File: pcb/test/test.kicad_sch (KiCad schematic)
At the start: 27 parts, among them IC1 ADG904BRUZ-REEL7, J1 CONSMA013.062-G, J3 Conn_01x04, U2 TL081

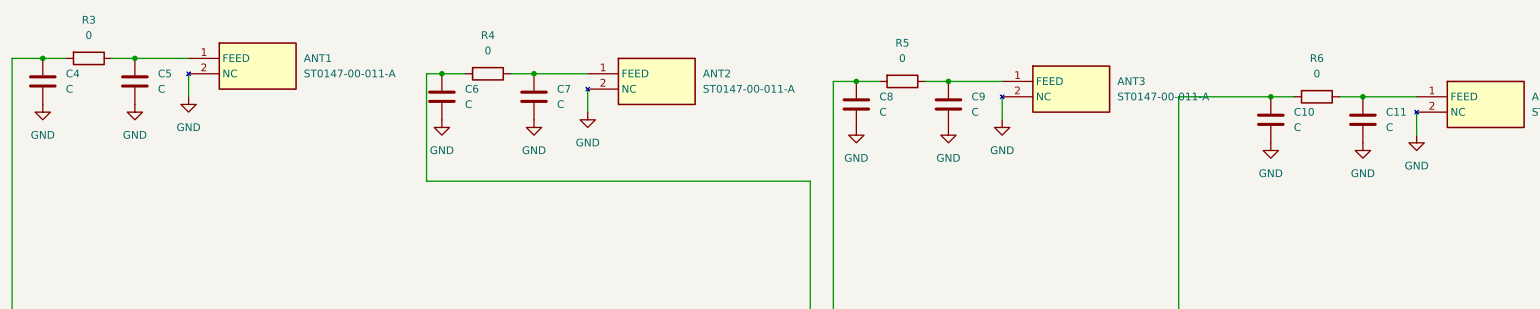
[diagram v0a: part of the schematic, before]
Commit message: routage guides d'onde
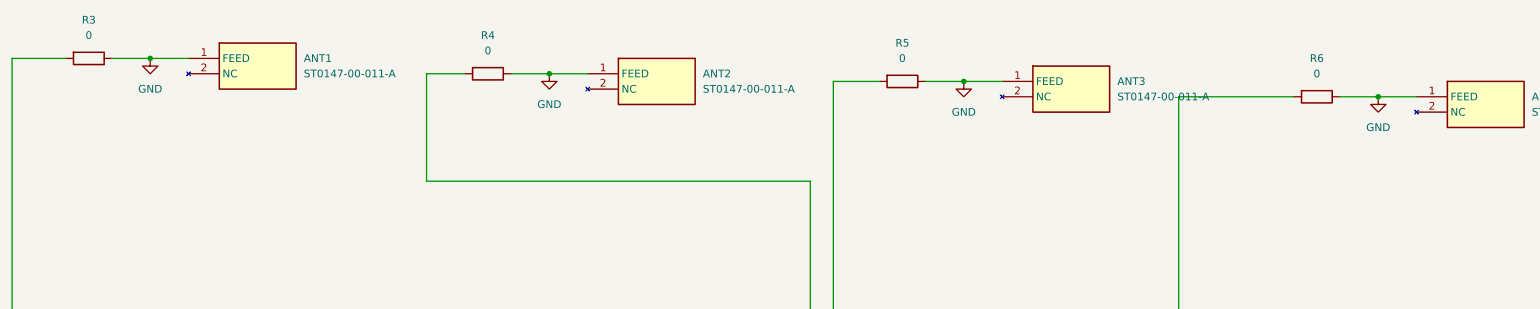
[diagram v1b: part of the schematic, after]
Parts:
- removed C10, C11, C4, C5, C6, C7, C8, C9: C, Capacitor_SMD:C_0201_0603Metric, symbol Device:C
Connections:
- net GND: now also ANT1.1 (FEED), ANT2.1 (FEED), ANT3.1 (FEED), ANT4.1 (FEED), R3.1, R4.1, R5.1, R6.1; no longer ANT1.2 (NC), ANT2.2 (NC), ANT3.2 (NC), ANT4.2 (NC)

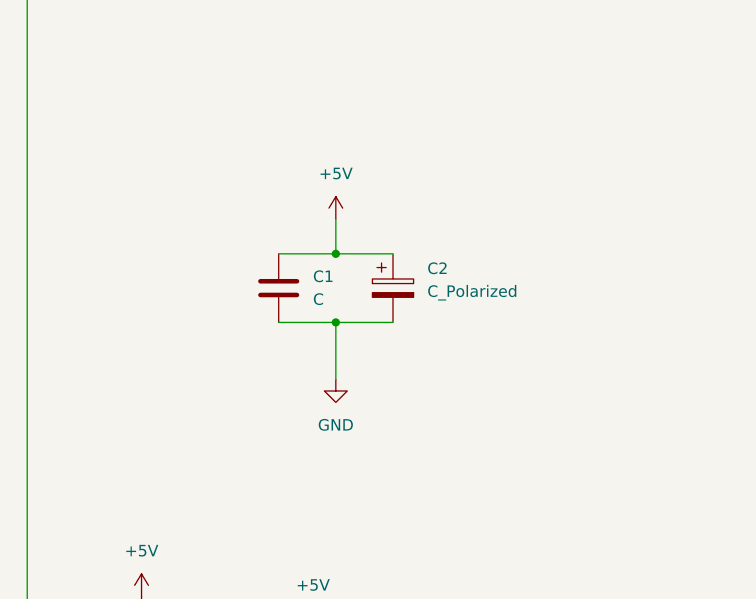
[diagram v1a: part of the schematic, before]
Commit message: composants pour 2V5 placés
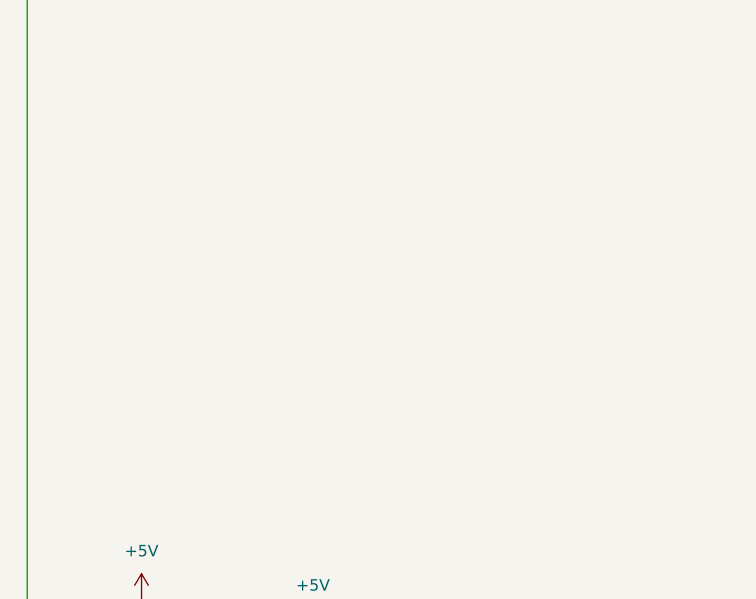
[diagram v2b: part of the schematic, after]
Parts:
- removed C1: C, Capacitor_SMD:CP_Elec_6.3x5.4, symbol Device:C
- removed C2: C_Polarized, Capacitor_SMD:CP_Elec_6.3x5.4, symbol Device:C_Polarized
- C3: footprint Capacitor_SMD:CP_Elec_6.3x5.4 -> Capacitor_THT:CP_Radial_D8.0mm_P5.00mm

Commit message: beaucoup vias
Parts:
- removed JP2: Jumper_2_Bridged, test_footprint_library:jumper20, symbol Jumper:Jumper_2_Bridged
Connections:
- net +2V5: now also JP1.1 (A); no longer IC1.2 (VDD)
- net +5V: now also J3.2 (Pin_2); no longer J3.1 (Pin_1)
- net GND: now also J3.1 (Pin_1); no longer J3.2 (Pin_2)
- net at IC1.20 (A0): now also J3.4 (Pin_4)
- net at J3.3 (Pin_3): now also IC1.19 (A1)
- net at JP1.2 (B): now also IC1.2 (VDD); no longer J3.4 (Pin_4)
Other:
- moved on the sheet: JP1
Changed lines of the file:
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@@
-	(wire
-		(pts
-			(xy 170.18 180.34) (xy 162.56 180.34)
-		)
-		(stroke
-			(width 0)
-			(type default)
-		)
-	)
 	(wire
 		(pts
@@
 	(wire
 		(pts
-			(xy 148.59 182.88) (xy 146.05 182.88)
-		)
-		(stroke
-			(width 0)
-			(type default)
-		)
-	)
-	(wire
-		(pts
 			(xy 172.72 31.75) (xy 179.07 31.75)
 		)
@@
 	(wire
 		(pts
-			(xy 162.56 180.34) (xy 162.56 189.23)
-		)
-		(stroke
-			(width 0)
-			(type default)
-		)
-	)
-	(wire
-		(pts
 			(xy 31.75 27.94) (xy 38.1 27.94)
 		)
@@
 	(wire
 		(pts
-			(xy 160.02 182.88) (xy 158.75 182.88)
-		)
-		(stroke
-			(width 0)
-			(type default)
-		)
-	)
-	(wire
-		(pts
 			(xy 140.97 143.51) (xy 148.59 143.51)
 		)
@@
 	(wire
 		(pts
-			(xy 146.05 182.88) (xy 146.05 123.19)
-		)
-		(stroke
-			(width 0)
-			(type default)
-		)
-	)
-	(wire
-		(pts
 			(xy 92.71 133.35) (xy 92.71 135.89)
 		)
@@
 	(wire
 		(pts
+			(xy 146.05 123.19) (xy 146.05 185.42)
+		)
+		(stroke
+			(width 0)
+			(type default)
+		)
+	)
+	(wire
+		(pts
+			(xy 165.1 189.23) (xy 165.1 187.96)
+		)
+		(stroke
+			(width 0)
+			(type default)
+		)
+	)
+	(wire
+		(pts
+			(xy 143.51 182.88) (xy 160.02 182.88)
+		)
+		(stroke
+			(width 0)
+			(type default)
+		)
+	)
+	(wire
+		(pts
 			(xy 99.06 138.43) (xy 99.06 161.29)
 		)
@@
 	(wire
 		(pts
-			(xy 71.12 128.27) (xy 81.28 128.27)
-		)
-		(stroke
-			(width 0)
-			(type default)
-		)
-	)
-	(wire
-		(pts
 			(xy 148.59 140.97) (xy 148.59 143.51)
 		)
@@
 	(wire
 		(pts
-			(xy 143.51 185.42) (xy 143.51 125.73)
-		)
-		(stroke
-			(width 0)
-			(type default)
-		)
-	)
-	(wire
-		(pts
 			(xy 151.13 161.29) (xy 151.13 31.75)
 		)
@@
 	(wire
 		(pts
-			(xy 157.48 185.42) (xy 154.94 185.42)
-		)
-		(stroke
-			(width 0)
-			(type default)
-		)
-	)
-	(wire
-		(pts
 			(xy 92.71 143.51) (xy 107.95 143.51)
 		)
@@
 	(wire
 		(pts
+			(xy 157.48 185.42) (xy 146.05 185.42)
+		)
+		(stroke
+			(width 0)
+			(type default)
+		)
+	)
+	(wire
+		(pts
 			(xy 148.59 135.89) (xy 148.59 140.97)
 		)
@@
 	(wire
 		(pts
-			(xy 165.1 189.23) (xy 173.99 189.23)
-		)
-		(stroke
-			(width 0)
-			(type default)
-		)
-	)
-	(wire
-		(pts
 			(xy 92.71 140.97) (xy 92.71 143.51)
 		)
@@
 	(wire
 		(pts
+			(xy 165.1 187.96) (xy 170.18 187.96)
+		)
+		(stroke
+			(width 0)
+			(type default)
+		)
+	)
+	(wire
+		(pts
 			(xy 92.71 116.84) (xy 92.71 123.19)
 		)
@@
 	(wire
 		(pts
+			(xy 143.51 182.88) (xy 143.51 125.73)
+		)
+		(stroke
+			(width 0)
+			(type default)
+		)
+	)
+	(wire
+		(pts
 			(xy 99.06 161.29) (xy 151.13 161.29)
 		)
@@
 	(wire
 		(pts
-			(xy 144.78 185.42) (xy 143.51 185.42)
-		)
-		(stroke
-			(width 0)
-			(type default)
-		)
-	)
-	(wire
-		(pts
 			(xy 83.82 48.26) (xy 83.82 30.48)
 		)
@@
 		(pts
 			(xy 208.28 138.43) (xy 208.28 34.29)
-		)
-		(stroke
-			(width 0)
-			(type default)
-		)
-	)
-	(wire
-		(pts
-			(xy 173.99 189.23) (xy 173.99 177.8)
 		)
 		(stroke
@@
 	)
 	(symbol
-		(lib_id "Jumper:Jumper_2_Bridged")
-		(at 153.67 182.88 0)
-		(unit 1)
-		(exclude_from_sim yes)
-		(in_bom yes)
-		(on_board yes)
-		(dnp no)
-		(fields_autoplaced yes)
-		(property "Reference" "JP2"
-			(at 153.67 177.8 0)
-			(effects
-				(font
-					(size 1.27 1.27)
-				)
-			)
-		)
-		(property "Value" "Jumper_2_Bridged"
-			(at 153.67 180.34 0)
-			(effects
-				(font
-					(size 1.27 1.27)
-				)
-				(hide yes)
-			)
-		)
-		(property "Footprint" "test_footprint_library:jumper20"
-			(at 153.67 182.88 0)
-			(effects
-				(font
-					(size 1.27 1.27)
-				)
-				(hide yes)
-			)
-		)
-		(property "Datasheet" "~"
-			(at 153.67 182.88 0)
-			(effects
-				(font
-					(size 1.27 1.27)
-				)
-				(hide yes)
-			)
-		)
-		(property "Description" "Jumper, 2-pole, closed/bridged"
-			(at 153.67 182.88 0)
-			(effects
-				(font
-					(size 1.27 1.27)
-				)
-				(hide yes)
-			)
-		)
-		(pin "2"
-		)
-		(pin "1"
-		)
-		(instances
-			(project "test"
-				(path "/bb1015a8-5dcf-444f-b1dc-3665f721c6b4"
-					(reference "JP2")
-					(unit 1)
-				)
-			)
-		)
-	)
-	(symbol
 		(lib_id "power:GND")
 		(at 241.3 34.29 0)
@@
 	(symbol
 		(lib_id "Jumper:Jumper_2_Bridged")
-		(at 149.86 185.42 0)
+		(at 76.2 128.27 0)
 		(unit 1)
 		(exclude_from_sim yes)
@@
 		(fields_autoplaced yes)
 		(property "Reference" "JP1"
-			(at 149.86 180.34 0)
+			(at 76.2 123.19 0)
 			(effects
 				(font
@@
 		)
 		(property "Value" "Jumper_2_Bridged"
-			(at 149.86 182.88 0)
+			(at 76.2 125.73 0)
 			(effects
 				(font
@@
 		)
 		(property "Footprint" "test_footprint_library:jumper20"
-			(at 149.86 185.42 0)
+			(at 76.2 128.27 0)
 			(effects
 				(font
@@
 		)
 		(property "Datasheet" "~"
-			(at 149.86 185.42 0)
+			(at 76.2 128.27 0)
 			(effects
 				(font
@@
 		)
 		(property "Description" "Jumper, 2-pole, closed/bridged"
-			(at 149.86 185.42 0)
+			(at 76.2 128.27 0)
 			(effects
 				(font
@@
 	(symbol
 		(lib_id "power:+5V")
-		(at 173.99 177.8 0)
+		(at 162.56 189.23 0)
 		(unit 1)
 		(exclude_from_sim no)
@@
 		(fields_autoplaced yes)
 		(property "Reference" "#PWR01"
-			(at 173.99 181.61 0)
+			(at 162.56 193.04 0)
 			(effects
 				(font
@@
 		)
 		(property "Value" "+5V"
-			(at 173.99 172.72 0)
+			(at 162.56 184.15 0)
 			(effects
 				(font
@@
 		)
 		(property "Footprint" ""
-			(at 173.99 177.8 0)
+			(at 162.56 189.23 0)
 			(effects
 				(font
@@
 		)
 		(property "Datasheet" ""
-			(at 173.99 177.8 0)
+			(at 162.56 189.23 0)
 			(effects
 				(font
@@
 		)
 		(property "Description" "Power symbol creates a global label with name \"+5V\""
-			(at 173.99 177.8 0)
+			(at 162.56 189.23 0)
 			(effects
 				(font
@@
 	(symbol
 		(lib_id "power:GND")
-		(at 170.18 180.34 0)
+		(at 170.18 187.96 0)
 		(unit 1)
 		(exclude_from_sim no)
@@
 		(fields_autoplaced yes)
 		(property "Reference" "#PWR08"
-			(at 170.18 186.69 0)
+			(at 170.18 194.31 0)
 			(effects
 				(font
@@
 		)
 		(property "Value" "GND"
-			(at 170.18 185.42 0)
+			(at 170.18 193.04 0)
 			(effects
 				(font
@@
 		)
 		(property "Footprint" ""
-			(at 170.18 180.34 0)
+			(at 170.18 187.96 0)
 			(effects
 				(font
@@
 		)
 		(property "Datasheet" ""
-			(at 170.18 180.34 0)
+			(at 170.18 187.96 0)
 			(effects
 				(font
@@
 		)
 		(property "Description" "Power symbol creates a global label with name \"GND\" , ground"
-			(at 170.18 180.34 0)
-			(effects
-				(font
+			(at 170.18 187.96 0)
+			(effects
+				(font

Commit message: céfini
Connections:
- net GND: now also ANT1.2 (NC), ANT2.2 (NC), ANT3.2 (NC), ANT4.2 (NC)

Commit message: ajustement pour impression
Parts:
- removed JP1: Jumper_2_Bridged, test_footprint_library:jumper20, symbol Jumper:Jumper_2_Bridged
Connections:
- net +2V5: now also IC1.2 (VDD)
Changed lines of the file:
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@@
+	(wire
+		(pts
+			(xy 71.12 128.27) (xy 81.28 128.27)
+		)
+		(stroke
+			(width 0)
+			(type default)
+		)
+	)
 	(wire
 		(pts
@@
 					(unit 1)
 				)
-			)
-		)
-	)
-	(symbol
-		(lib_id "Jumper:Jumper_2_Bridged")
-		(at 76.2 128.27 0)
-		(unit 1)
-		(exclude_from_sim yes)
-		(in_bom yes)
-		(on_board yes)
-		(dnp no)
-		(fields_autoplaced yes)
-		(property "Reference" "JP1"
-			(at 76.2 123.19 0)
-			(effects
-				(font
-					(size 1.27 1.27)
-				)
-			)
-		)
-		(property "Value" "Jumper_2_Bridged"
-			(at 76.2 125.73 0)
-			(effects
-				(font
-					(size 1.27 1.27)
-				)
-				(hide yes)
-			)
-		)
-		(property "Footprint" "test_footprint_library:jumper20"
-			(at 76.2 128.27 0)
-			(effects
-				(font
-					(size 1.27 1.27)
-				)
-				(hide yes)
-			)
-		)
-		(property "Datasheet" "~"
-			(at 76.2 128.27 0)
-			(effects
-				(font
-					(size 1.27 1.27)
-				)
-				(hide yes)
-			)
-		)
-		(property "Description" "Jumper, 2-pole, closed/bridged"
-			(at 76.2 128.27 0)
-			(effects
-				(font
-					(size 1.27 1.27)
-				)
-				(hide yes)
-			)
-		)
-		(pin "2"
-		)
-		(pin "1"
-		)
-		(instances
-			(project ""
-				(path "/bb1015a8-5dcf-444f-b1dc-3665f721c6b4"
-					(reference "JP1")
-					(unit 1)
-				)
